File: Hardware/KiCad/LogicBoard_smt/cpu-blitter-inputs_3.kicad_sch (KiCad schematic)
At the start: 68 parts

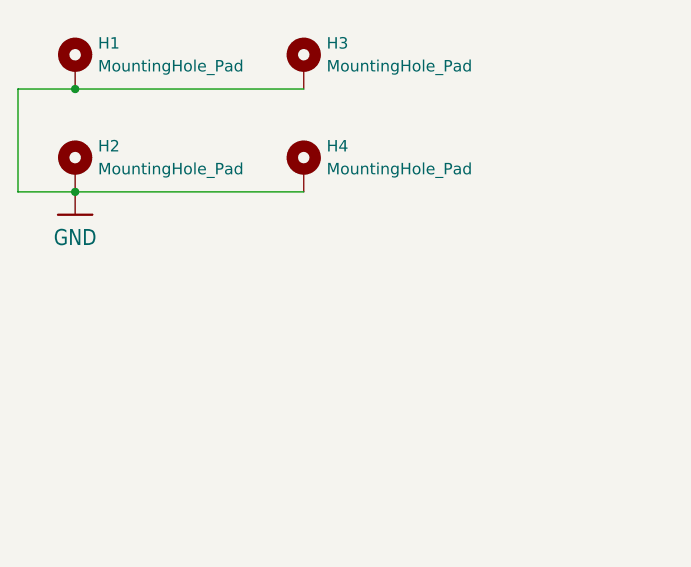
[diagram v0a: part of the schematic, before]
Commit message: updates to kicad smt versions
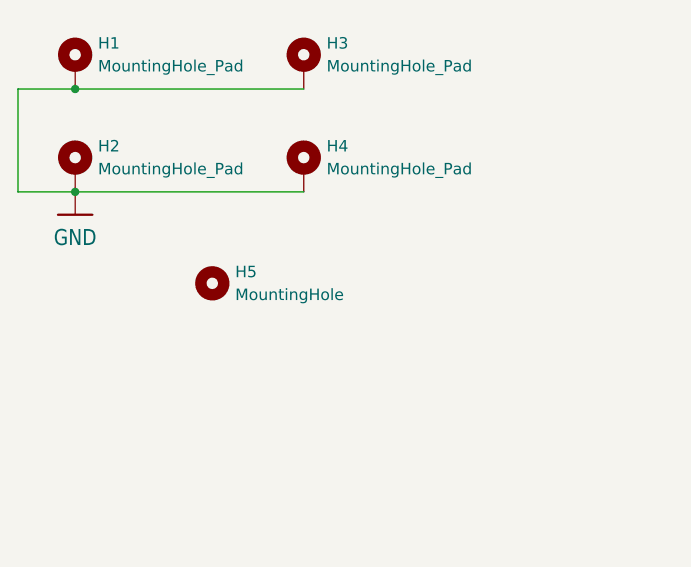
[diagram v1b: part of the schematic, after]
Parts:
- added H5: MountingHole, MountingHole:MountingHole_3.2mm_M3, symbol Mechanical:MountingHole
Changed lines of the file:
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@@
+    )
+  )
+  (symbol (lib_id "Mechanical:MountingHole") (at 54.61 71.12 0) (unit 1)
+    (in_bom yes) (on_board yes) (dnp no) (fields_autoplaced)
+    (property "Reference" "H5" (at 57.15 69.85 0)
+      (effects (font (size 1.27 1.27)) (justify left))
+    )
+    (property "Value" "MountingHole" (at 57.15 72.39 0)
+      (effects (font (size 1.27 1.27)) (justify left))
+    )
+    (property "Footprint" "MountingHole:MountingHole_3.2mm_M3" (at 54.61 71.12 0)
+      (effects (font (size 1.27 1.27)) hide)
+    )
+    (property "Datasheet" "~" (at 54.61 71.12 0)
+      (effects (font (size 1.27 1.27)) hide)
+    )
+    (instances
+      (project "LogicBoard_smt"
+        (path "/28034957-81b4-48a5-b869-6f4cb8f0c2fa/95bc2f6c-a227-442d-9d58-41fddaf17fd9"
+          (reference "H5") (unit 1)
+        )
+      )
     )
   )

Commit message: manual and models and misc hardware file updates
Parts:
- removed +5V0, GROUND0: 3,81/1,4, cpu-blitter-inputs:3,81_1,4, symbol cpu-blitter-inputs-eagle-import:3,81/1,4
- removed H5: MountingHole, MountingHole:MountingHole_3.2mm_M3, symbol Mechanical:MountingHole
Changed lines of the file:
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@@
-    )
-  )
-  (symbol (lib_id "cpu-blitter-inputs-eagle-import:3,81/1,4") (at 73.66 154.94 0) (unit 1)
-    (in_bom yes) (on_board yes) (dnp no)
-    (property "Reference" "+5V0" (at 69.977 153.0858 0)
-      (effects (font (size 1.778 1.5113)) (justify left bottom))
-    )
-    (property "Value" "3,81/1,4" (at 72.517 158.242 0)
-      (effects (font (size 1.778 1.5113)) (justify left bottom) hide)
-    )
-    (property "Footprint" "cpu-blitter-inputs:3,81_1,4" (at 73.66 154.94 0)
-      (effects (font (size 1.27 1.27)) hide)
-    )
-    (property "Datasheet" "" (at 73.66 154.94 0)
-      (effects (font (size 1.27 1.27)) hide)
-    )
-    (property "MPN" "DNI" (at 73.66 154.94 0)
-      (effects (font (size 1.27 1.27)) hide)
-    )
-    (pin "1")
-    (instances
-      (project "LogicBoard_smt"
-        (path "/28034957-81b4-48a5-b869-6f4cb8f0c2fa/95bc2f6c-a227-442d-9d58-41fddaf17fd9"
-          (reference "+5V0") (unit 1)
-        )
-      )
     )
   )
@@
     )
   )
-  (symbol (lib_id "cpu-blitter-inputs-eagle-import:GND") (at 66.04 162.56 0) (unit 1)
-    (in_bom yes) (on_board yes) (dnp no)
-    (property "Reference" "#GND033" (at 66.04 162.56 0)
-      (effects (font (size 1.27 1.27)) hide)
-    )
-    (property "Value" "GND" (at 63.5 165.1 0)
-      (effects (font (size 1.778 1.5113)) (justify left bottom))
-    )
-    (property "Footprint" "" (at 66.04 162.56 0)
-      (effects (font (size 1.27 1.27)) hide)
-    )
-    (property "Datasheet" "" (at 66.04 162.56 0)
-      (effects (font (size 1.27 1.27)) hide)
-    )
-    (pin "1")
-    (instances
-      (project "LogicBoard_smt"
-        (path "/28034957-81b4-48a5-b869-6f4cb8f0c2fa/95bc2f6c-a227-442d-9d58-41fddaf17fd9"
-          (reference "#GND033") (unit 1)
-        )
-      )
-    )
-  )
   (symbol (lib_id "cpu-blitter-inputs-eagle-import:C-US025-024X044") (at 187.96 86.36 0) (unit 1)
     (in_bom yes) (on_board yes) (dnp no)
@@
         (path "/28034957-81b4-48a5-b869-6f4cb8f0c2fa/95bc2f6c-a227-442d-9d58-41fddaf17fd9"
           (reference "C28") (unit 1)
-        )
-      )
-    )
-  )
-  (symbol (lib_id "Mechanical:MountingHole") (at 54.61 71.12 0) (unit 1)
-    (in_bom yes) (on_board yes) (dnp no) (fields_autoplaced)
-    (property "Reference" "H5" (at 57.15 69.85 0)
-      (effects (font (size 1.27 1.27)) (justify left))
-    )
-    (property "Value" "MountingHole" (at 57.15 72.39 0)
-      (effects (font (size 1.27 1.27)) (justify left))
-    )
-    (property "Footprint" "MountingHole:MountingHole_3.2mm_M3" (at 54.61 71.12 0)
-      (effects (font (size 1.27 1.27)) hide)
-    )
-    (property "Datasheet" "~" (at 54.61 71.12 0)
-      (effects (font (size 1.27 1.27)) hide)
-    )
-    (instances
-      (project "LogicBoard_smt"
-        (path "/28034957-81b4-48a5-b869-6f4cb8f0c2fa/95bc2f6c-a227-442d-9d58-41fddaf17fd9"
-          (reference "H5") (unit 1)
         )
       )
@@
     )
   )
-  (symbol (lib_id "cpu-blitter-inputs-eagle-import:3,81/1,4") (at 66.04 157.48 270) (unit 1)
-    (in_bom yes) (on_board yes) (dnp no)
-    (property "Reference" "GROUND0" (at 66.7258 156.083 0)
-      (effects (font (size 1.778 1.5113)) (justify right top))
-    )
-    (property "Value" "3,81/1,4" (at 62.738 156.337 0)
-      (effects (font (size 1.778 1.5113)) (justify left bottom) hide)
-    )
-    (property "Footprint" "cpu-blitter-inputs:3,81_1,4" (at 66.04 157.48 0)
-      (effects (font (size 1.27 1.27)) hide)
-    )
-    (property "Datasheet" "" (at 66.04 157.48 0)
-      (effects (font (size 1.27 1.27)) hide)
-    )
-    (property "MPN" "DNI" (at 66.04 157.48 0)
-      (effects (font (size 1.27 1.27)) hide)
-    )
-    (pin "1")
-    (instances
-      (project "LogicBoard_smt"
-        (path "/28034957-81b4-48a5-b869-6f4cb8f0c2fa/95bc2f6c-a227-442d-9d58-41fddaf17fd9"
-          (reference "GROUND0") (unit 1)
-        )
-      )
-    )
-  )
   (symbol (lib_id "cpu-blitter-inputs-eagle-import:C-US025-024X044") (at 149.86 96.52 0) (unit 1)
     (in_bom yes) (on_board yes) (dnp no)
@@
         )
       )
-    )
-  )
-  (symbol (lib_id "cpu-blitter-inputs-eagle-import:VCC") (at 78.74 154.94 270) (unit 1)
-    (in_bom yes) (on_board yes) (dnp no)
-    (property "Reference" "#P+037" (at 78.74 154.94 0)
-      (effects (font (size 1.27 1.27)) hide)
-    )
-    (property "Value" "VCC" (at 76.2 152.4 90)
-      (effects (font (size 1.778 1.5113)) (justify left bottom))
-    )
-    (property "Footprint" "" (at 78.74 154.94 0)
-      (effects (font (size 1.27 1.27)) hide)
-    )
-    (property "Datasheet" "" (at 78.74 154.94 0)
-      (effects (font (size 1.27 1.27)) hide)
-    )
-    (pin "1")
-    (instances
-      (project "LogicBoard_smt"
-        (path "/28034957-81b4-48a5-b869-6f4cb8f0c2fa/95bc2f6c-a227-442d-9d58-41fddaf17fd9"
-          (reference "#P+037") (unit 1)
-        )
-      )

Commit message: updates
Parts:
- LED1: footprint Connector_PinHeader_2.54mm:PinHeader_1x02_P2.54mm_Vertical_SMD_Pin1Right -> Connector_PinHeader_2.54mm:PinHeader_1x02_P2.54mm_Vertical; MPN TSM-102-01-L-SV-TR -> G800WC306018EU
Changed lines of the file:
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@@
 			)
 		)
-		(property "Footprint" "Connector_PinHeader_2.54mm:PinHeader_1x02_P2.54mm_Vertical_SMD_Pin1Right"
+		(property "Footprint" "Connector_PinHeader_2.54mm:PinHeader_1x02_P2.54mm_Vertical"
 			(at 134.62 165.1 0)
 			(effects
@@
 			)
 		)
-		(property "MPN" "TSM-102-01-L-SV-TR"
+		(property "MPN" "G800WC306018EU "
 			(at 134.62 165.1 0)
 			(effects
